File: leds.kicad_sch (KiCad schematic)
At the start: 36 parts

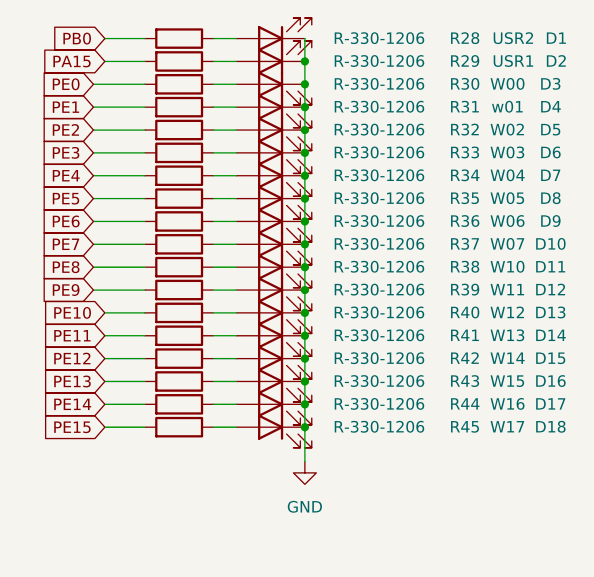
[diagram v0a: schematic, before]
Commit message: Working on the limiter
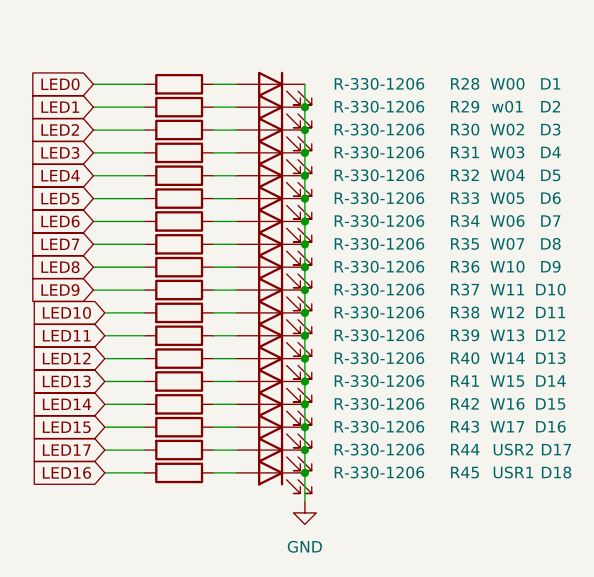
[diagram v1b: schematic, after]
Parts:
- renumbered D3 to D1, D12 to D10, D13 to D11, D14 to D12, D15 to D13, D16 to D14, D17 to D15, D18 to D16, D1 to D17, D2 to D18, D4 to D2, D5 to D3, D6 to D4, D7 to D5, D8 to D6, D9 to D7, D10 to D8, D11 to D9, R30 to R28, R31 to R29, R32 to R30, R33 to R31, R34 to R32, R35 to R33, R36 to R34, R37 to R35, R38 to R36, R39 to R37, R40 to R38, R41 to R39, R42 to R40, R43 to R41, R44 to R42, R45 to R43, R28 to R44, R29 to R45
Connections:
- net PA15 renamed LED16
- net PB0 renamed LED17
- net PE0 renamed LED0
- net PE1 renamed LED1
- net PE10 renamed LED10
- net PE11 renamed LED11
- net PE12 renamed LED12
- net PE13 renamed LED13
- net PE14 renamed LED14
- net PE15 renamed LED15
- net PE2 renamed LED2
- net PE3 renamed LED3
- net PE4 renamed LED4
- net PE5 renamed LED5
- net PE6 renamed LED6
- net PE7 renamed LED7
- net PE8 renamed LED8
- net PE9 renamed LED9
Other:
- moved on the sheet: D17, D18, R44, R45

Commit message: working on AD inputs
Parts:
- renumbered D3 to D10, D4 to D11, D5 to D12, D6 to D13, D7 to D14, D8 to D15, D9 to D16, D10 to D17, D11 to D18, D12 to D19, D13 to D20, D14 to D21, D15 to D22, D16 to D23, D17 to D24, D18 to D25, D1 to D8, D2 to D9, R28 to R42, R29 to R43, R30 to R44, R31 to R45, R32 to R46, R33 to R47, R34 to R48, R35 to R49, R36 to R50, R37 to R51, R38 to R52, R39 to R53, R40 to R54, R41 to R55, R42 to R56, R43 to R57, R44 to R58, R45 to R59

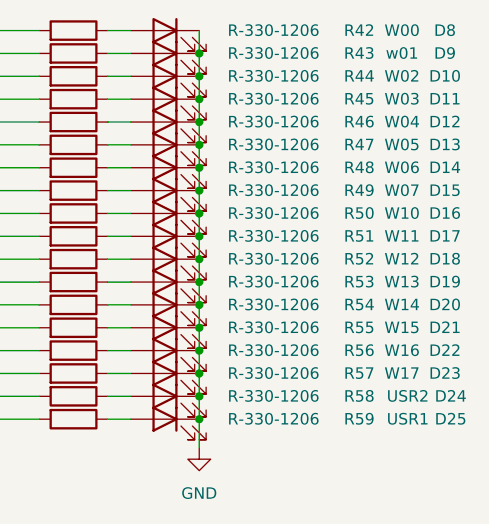
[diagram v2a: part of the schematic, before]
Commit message: reannotated changed to LM324
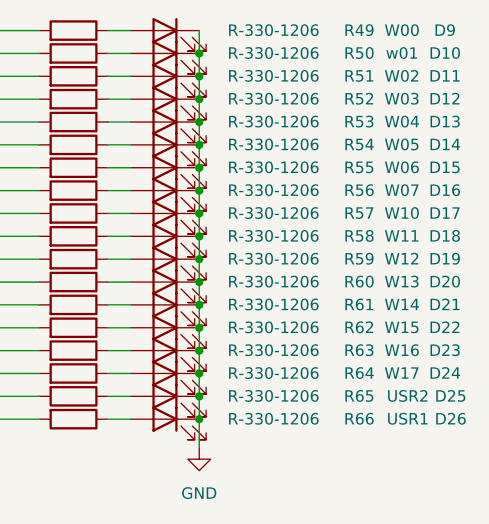
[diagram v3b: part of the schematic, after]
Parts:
- renumbered D9 to D10, D10 to D11, D11 to D12, D12 to D13, D13 to D14, D14 to D15, D15 to D16, D16 to D17, D17 to D18, D18 to D19, D19 to D20, D20 to D21, D21 to D22, D22 to D23, D23 to D24, D24 to D25, D25 to D26, D8 to D9, R42 to R49, R43 to R50, R44 to R51, R45 to R52, R46 to R53, R47 to R54, R48 to R55, R49 to R56, R50 to R57, R51 to R58, R52 to R59, R53 to R60, R54 to R61, R55 to R62, R56 to R63, R57 to R64, R58 to R65, R59 to R66

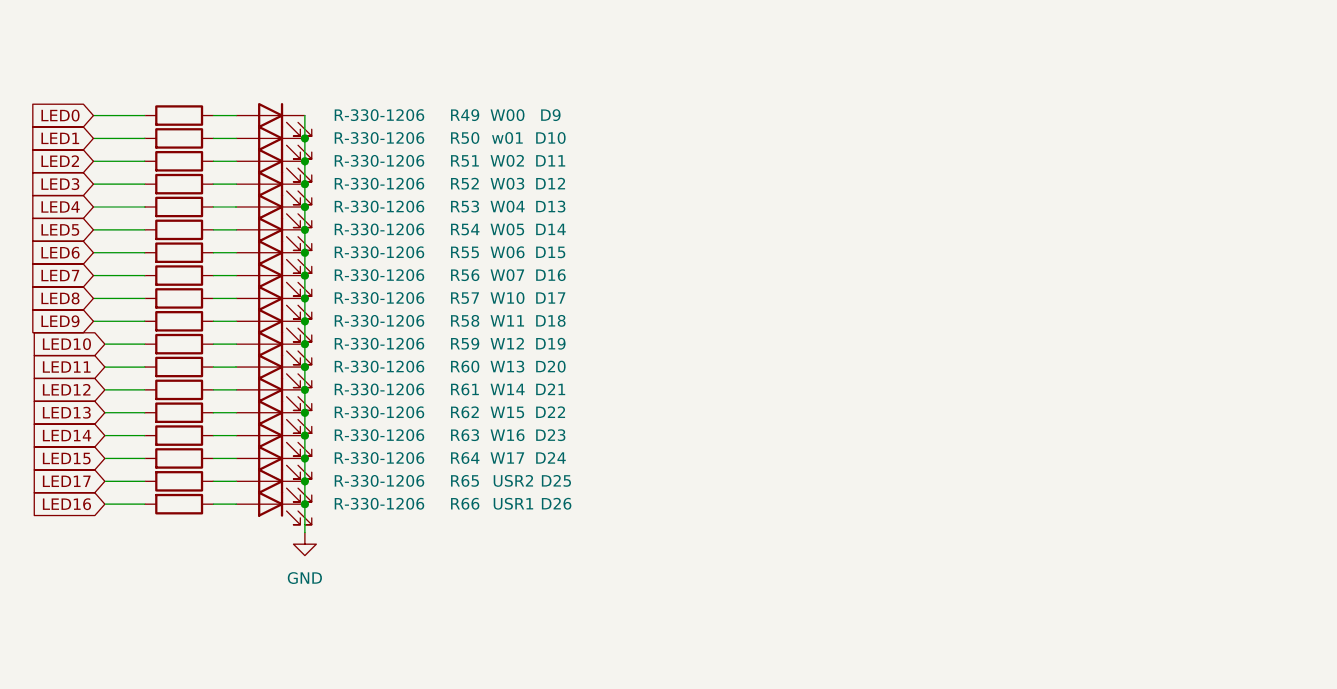
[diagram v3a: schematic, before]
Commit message: working on lifted leds
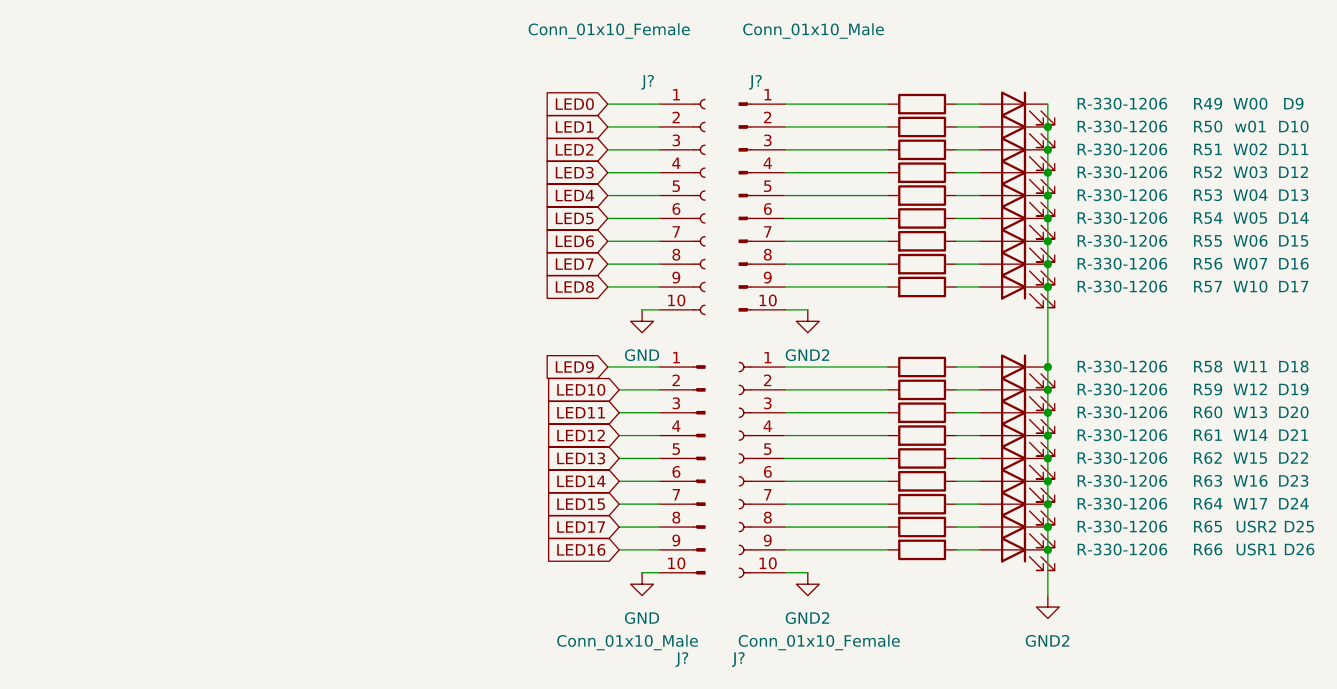
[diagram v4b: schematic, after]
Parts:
- added J? (x2): Conn_01x10_Male, symbol Connector:Conn_01x10_Male
- added J? (x2): Conn_01x10_Female, symbol Connector:Conn_01x10_Female
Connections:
- net GND: now also J?.10 (Pin_10), J?.10 (Pin_10); no longer D10.1 (K), D11.1 (K), D12.1 (K), D13.1 (K), D14.1 (K), D15.1 (K), D16.1 (K), D17.1 (K), D18.1 (K), D19.1 (K), D20.1 (K), D21.1 (K), D22.1 (K), D23.1 (K), D24.1 (K), D25.1 (K), D26.1 (K), D9.1 (K)
- net LED0: now also J?.1 (Pin_1); no longer R49.2
- net LED1: now also J?.2 (Pin_2); no longer R50.2
- net LED10: now also J?.2 (Pin_2); no longer R59.2
- net LED11: now also J?.3 (Pin_3); no longer R60.2
- net LED12: now also J?.4 (Pin_4); no longer R61.2
- net LED13: now also J?.5 (Pin_5); no longer R62.2
- net LED14: now also J?.6 (Pin_6); no longer R63.2
- net LED15: now also J?.7 (Pin_7); no longer R64.2
- net LED16: now also J?.9 (Pin_9); no longer R66.2
- net LED17: now also J?.8 (Pin_8); no longer R65.2
- net LED2: now also J?.3 (Pin_3); no longer R51.2
- net LED3: now also J?.4 (Pin_4); no longer R52.2
- net LED4: now also J?.5 (Pin_5); no longer R53.2
- net LED5: now also J?.6 (Pin_6); no longer R54.2
- net LED6: now also J?.7 (Pin_7); no longer R55.2
- net LED7: now also J?.8 (Pin_8); no longer R56.2
- net LED8: now also J?.9 (Pin_9); no longer R57.2
- net LED9: now also J?.1 (Pin_1); no longer R58.2
- new net: J?.4 (Pin_4), R52.2
- new net: J?.1 (Pin_1), R49.2
- new net: J?.2 (Pin_2), R50.2
- new net: J?.3 (Pin_3), R51.2
- new net: J?.5 (Pin_5), R53.2
- new net: J?.6 (Pin_6), R54.2
- new net: J?.7 (Pin_7), R55.2
- new net: J?.8 (Pin_8), R56.2
- new net: J?.9 (Pin_9), R57.2
- new net: J?.9 (Pin_9), R66.2
- new net: J?.1 (Pin_1), R58.2
- new net: J?.2 (Pin_2), R59.2
- new net: J?.4 (Pin_4), R61.2
- new net: J?.8 (Pin_8), R65.2
- new net: J?.7 (Pin_7), R64.2
- new net: J?.6 (Pin_6), R63.2
- new net: J?.3 (Pin_3), R60.2
- new net: J?.5 (Pin_5), R62.2
- new net GND2: D10.1 (K), D11.1 (K), D12.1 (K), D13.1 (K), D14.1 (K), D15.1 (K), D16.1 (K), D17.1 (K), D18.1 (K), D19.1 (K), D20.1 (K), D21.1 (K), D22.1 (K), D23.1 (K), D24.1 (K), D25.1 (K), D26.1 (K), D9.1 (K), J?.10 (Pin_10), J?.10 (Pin_10)
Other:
- moved on the sheet: D10, D11, D12, D13, D14, D15, D16, D17, D18, D19, D20, D21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

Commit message: wip led panel
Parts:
- J3: renamed from J?; footprint (none) -> Connector_PinHeader_2.54mm:PinHeader_1x10_P2.54mm_Vertical
- J4: renamed from J?; footprint (none) -> Connector_PinHeader_2.54mm:PinHeader_2x05_P2.54mm_Vertical
- J5: renamed from J?; footprint (none) -> Connector_PinSocket_2.54mm:PinSocket_1x10_P2.54mm_Vertical
- J6: renamed from J?; footprint (none) -> Connector_PinSocket_2.54mm:PinSocket_2x05_P2.54mm_Vertical
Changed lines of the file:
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@@
   (symbol (lib_id "Connector:Conn_01x10_Male") (at 102.235 38.1 0) (unit 1)
     (in_bom yes) (on_board yes)
-    (property "Reference" "J?" (id 0) (at 104.14 25.4 0))
+    (property "Reference" "J5" (id 0) (at 104.14 25.4 0))
     (property "Value" "Conn_01x10_Male" (id 1) (at 110.49 19.685 0))
-    (property "Footprint" "" (id 2) (at 102.235 38.1 0)
+    (property "Footprint" "Connector_PinSocket_2.54mm:PinSocket_1x10_P2.54mm_Vertical" (id 2) (at 102.235 38.1 0)
       (effects (font (size 1.27 1.27)) hide)
     )
@@
   (symbol (lib_id "power:GND2") (at 109.855 50.8 0) (unit 1)
     (in_bom yes) (on_board yes) (fields_autoplaced)
-    (property "Reference" "#PWR?" (id 0) (at 109.855 57.15 0)
+    (property "Reference" "#PWR0126" (id 0) (at 109.855 57.15 0)
       (effects (font (size 1.27 1.27)) hide)
     )
@@
   (symbol (lib_id "power:GND2") (at 109.855 80.01 0) (unit 1)
     (in_bom yes) (on_board yes) (fields_autoplaced)
-    (property "Reference" "#PWR?" (id 0) (at 109.855 86.36 0)
+    (property "Reference" "#PWR0125" (id 0) (at 109.855 86.36 0)
       (effects (font (size 1.27 1.27)) hide)
     )
@@
   (symbol (lib_id "Connector:Conn_01x10_Male") (at 98.425 67.31 0) (mirror y) (unit 1)
     (in_bom yes) (on_board yes)
-    (property "Reference" "J?" (id 0) (at 95.25 89.535 0)
+    (property "Reference" "J4" (id 0) (at 95.25 89.535 0)
       (effects (font (size 1.27 1.27)) (justify right))
     )
@@
       (effects (font (size 1.27 1.27)) (justify right))
     )
-    (property "Footprint" "" (id 2) (at 98.425 67.31 0)
+    (property "Footprint" "Connector_PinHeader_2.54mm:PinHeader_2x05_P2.54mm_Vertical" (id 2) (at 98.425 67.31 0)
       (effects (font (size 1.27 1.27)) hide)
     )
@@
   (symbol (lib_id "power:GND") (at 91.44 80.01 0) (unit 1)
     (in_bom yes) (on_board yes) (fields_autoplaced)
-    (property "Reference" "#PWR?" (id 0) (at 91.44 86.36 0)
+    (property "Reference" "#PWR0124" (id 0) (at 91.44 86.36 0)
       (effects (font (size 1.27 1.27)) hide)
     )
@@
   (symbol (lib_id "Connector:Conn_01x10_Female") (at 98.425 38.1 0) (unit 1)
     (in_bom yes) (on_board yes)
-    (property "Reference" "J?" (id 0) (at 91.44 25.4 0)
+    (property "Reference" "J3" (id 0) (at 91.44 25.4 0)
       (effects (font (size 1.27 1.27)) (justify left))
     )
@@
       (effects (font (size 1.27 1.27)) (justify left))
     )
-    (property "Footprint" "" (id 2) (at 98.425 38.1 0)
+    (property "Footprint" "Connector_PinHeader_2.54mm:PinHeader_1x10_P2.54mm_Vertical" (id 2) (at 98.425 38.1 0)
       (effects (font (size 1.27 1.27)) hide)
     )
@@
   (symbol (lib_id "power:GND2") (at 136.525 82.55 0) (unit 1)
     (in_bom yes) (on_board yes) (fields_autoplaced)
-    (property "Reference" "#PWR?" (id 0) (at 136.525 88.9 0)
+    (property "Reference" "#PWR0127" (id 0) (at 136.525 88.9 0)
       (effects (font (size 1.27 1.27)) hide)
     )
@@
   (symbol (lib_id "power:GND") (at 91.44 50.8 0) (unit 1)
     (in_bom yes) (on_board yes) (fields_autoplaced)
-    (property "Reference" "#PWR?" (id 0) (at 91.44 57.15 0)
+    (property "Reference" "#PWR0123" (id 0) (at 91.44 57.15 0)
       (effects (font (size 1.27 1.27)) hide)
     )
@@
   (symbol (lib_id "Connector:Conn_01x10_Female") (at 102.235 67.31 0) (mirror y) (unit 1)
     (in_bom yes) (on_board yes)
-    (property "Reference" "J?" (id 0) (at 102.235 89.535 0))
+    (property "Reference" "J6" (id 0) (at 102.235 89.535 0))
     (property "Value" "Conn_01x10_Female" (id 1) (at 111.125 87.63 0))
-    (property "Footprint" "" (id 2) (at 102.235 67.31 0)
-      (effects (font (size 1.27 1.27)) hide)
-    )
+    (property "Footprint" "Connector_PinSocket_2.54mm:PinSocket_2x05_P2.54mm_Vertical" (id 2) (at 102.235 67.31 0)
+      (effects (font (size 1.27 1.27)) hide)
+    )

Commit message: yet an other new version with 3 boards
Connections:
- net GND renamed GND3
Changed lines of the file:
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@@
     (pin "2")
+  )
+  (symbol (lib_id "power:GND3") (at 91.44 80.01 0) (unit 1)
+    (in_bom yes) (on_board yes) (fields_autoplaced)
+    (property "Reference" "#PWR0124" (id 0) (at 91.44 86.36 0)
+      (effects (font (size 1.27 1.27)) hide)
+    )
+    (property "Value" "GND3" (id 1) (at 91.44 85.09 0))
+    (property "Footprint" "" (id 2) (at 91.44 80.01 0)
+      (effects (font (size 1.27 1.27)) hide)
+    )
+    (property "Datasheet" "" (id 3) (at 91.44 80.01 0)
+      (effects (font (size 1.27 1.27)) hide)
+    )
+    (pin "1")
   )
   (symbol (lib_id "power:GND2") (at 109.855 50.8 0) (unit 1)
@@
     (pin "1")
     (pin "2")
+  )
+  (symbol (lib_id "power:GND3") (at 91.44 50.8 0) (unit 1)
+    (in_bom yes) (on_board yes) (fields_autoplaced)
+    (property "Reference" "#PWR0123" (id 0) (at 91.44 57.15 0)
+      (effects (font (size 1.27 1.27)) hide)
+    )
+    (property "Value" "GND3" (id 1) (at 91.44 55.88 0))
+    (property "Footprint" "" (id 2) (at 91.44 50.8 0)
+      (effects (font (size 1.27 1.27)) hide)
+    )
+    (property "Datasheet" "" (id 3) (at 91.44 50.8 0)
+      (effects (font (size 1.27 1.27)) hide)
+    )
+    (pin "1")
   )
   (symbol (lib_id "eurorack:R-330-1206") (at 122.555 59.69 270) (mirror x) (unit 1)
@@
     (pin "2")
   )
-  (symbol (lib_id "power:GND") (at 91.44 80.01 0) (unit 1)
-    (in_bom yes) (on_board yes) (fields_autoplaced)
-    (property "Reference" "#PWR0124" (id 0) (at 91.44 86.36 0)
-      (effects (font (size 1.27 1.27)) hide)
-    )
-    (property "Value" "GND" (id 1) (at 91.44 85.09 0))
-    (property "Footprint" "" (id 2) (at 91.44 80.01 0)
-      (effects (font (size 1.27 1.27)) hide)
-    )
-    (property "Datasheet" "" (id 3) (at 91.44 80.01 0)
-      (effects (font (size 1.27 1.27)) hide)
-    )
-    (pin "1")
-  )
   (symbol (lib_id "Device:LED") (at 132.715 43.18 0) (mirror y) (unit 1)
     (in_bom yes) (on_board yes)
@@
     (pin "2")
   )
-  (symbol (lib_id "power:GND") (at 91.44 50.8 0) (unit 1)
-    (in_bom yes) (on_board yes) (fields_autoplaced)
-    (property "Reference" "#PWR0123" (id 0) (at 91.44 57.15 0)
-      (effects (font (size 1.27 1.27)) hide)
-    )
-    (property "Value" "GND" (id 1) (at 91.44 55.88 0))
-    (property "Footprint" "" (id 2) (at 91.44 50.8 0)
-      (effects (font (size 1.27 1.27)) hide)
-    )
-    (property "Datasheet" "" (id 3) (at 91.44 50.8 0)
-      (effects (font (size 1.27 1.27)) hide)
-    )
-    (pin "1")
-  )
   (symbol (lib_id "eurorack:R-330-1206") (at 122.555 43.18 270) (mirror x) (unit 1)
